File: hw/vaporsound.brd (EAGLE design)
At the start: 100 x 80 mm, 83 parts, among them P9 MA23-2, Q1 BSS138, Q2 BSS138

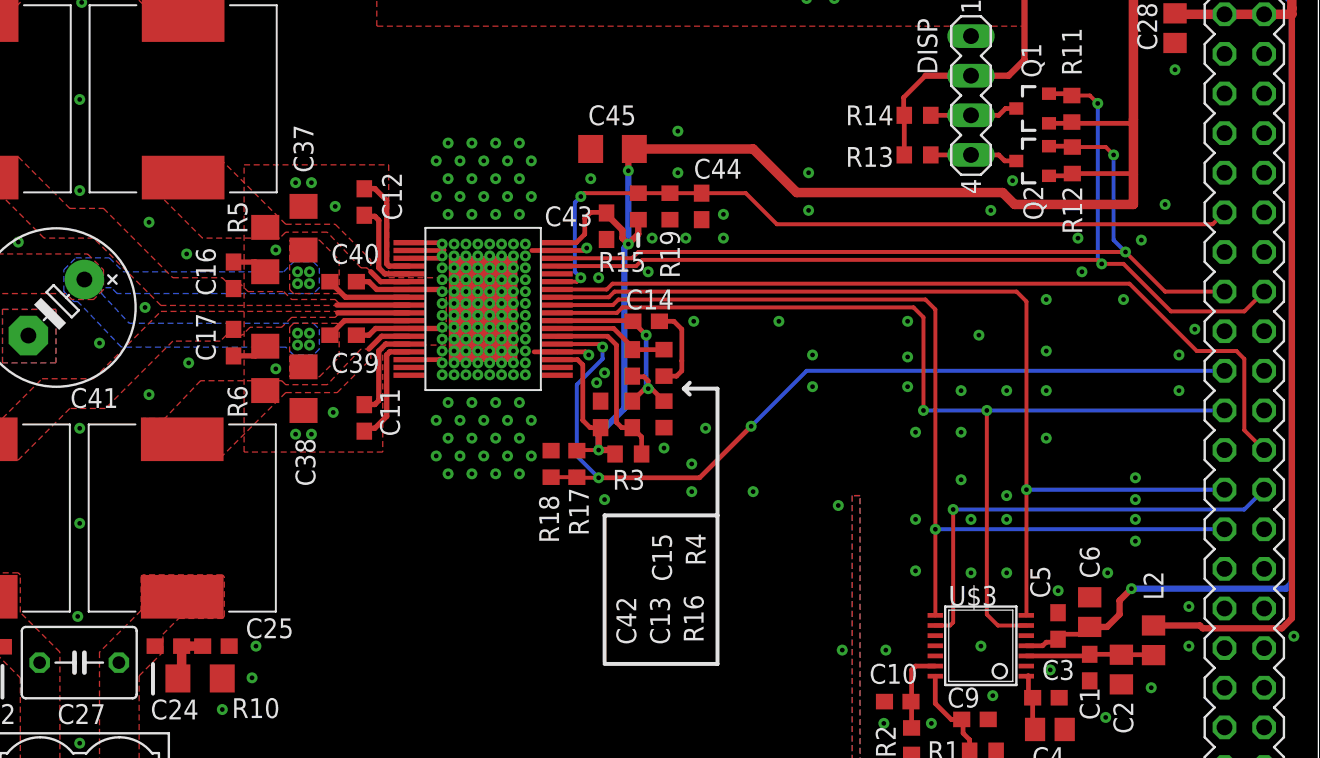
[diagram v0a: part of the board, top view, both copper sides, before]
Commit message: changes for easier manufacturability
minimum trace width 8mil
minimum clearance 7mil (8mil except the sta350bw)
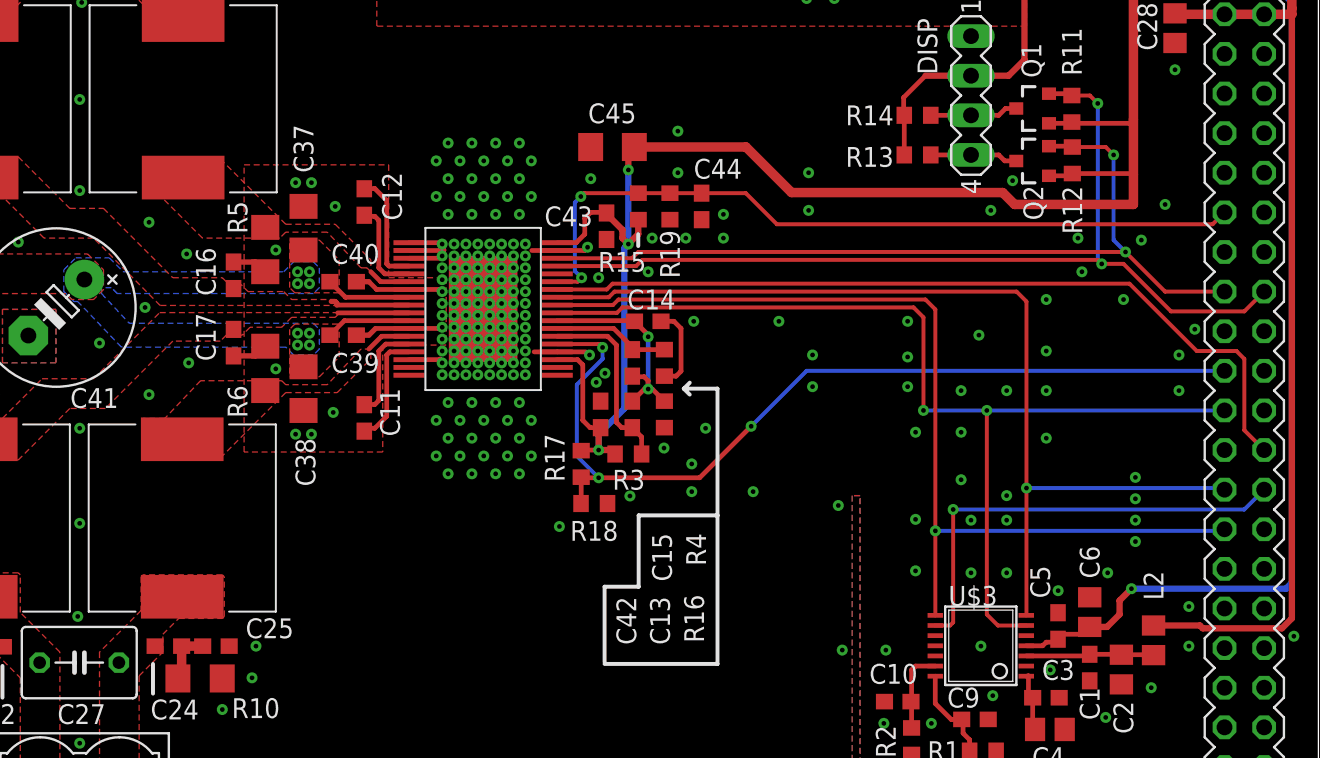
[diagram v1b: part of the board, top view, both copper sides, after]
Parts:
- moved R18 3.76 mm to (53.6, 28.3), turned to 0 degrees
- moved R17 0.28 mm to (52.7, 30.9)
- moved C45 0.13 mm to (54.7, 51.2)
- moved C14 0.10 mm to (57.0, 40.0)
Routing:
- net POWERDOWN: track 59.4 -> 58.4 mm
- net OUT2A: track 4.63 -> 5.16 mm
- net GND: track 27.0 -> 26.8 mm, vias 355 -> 356

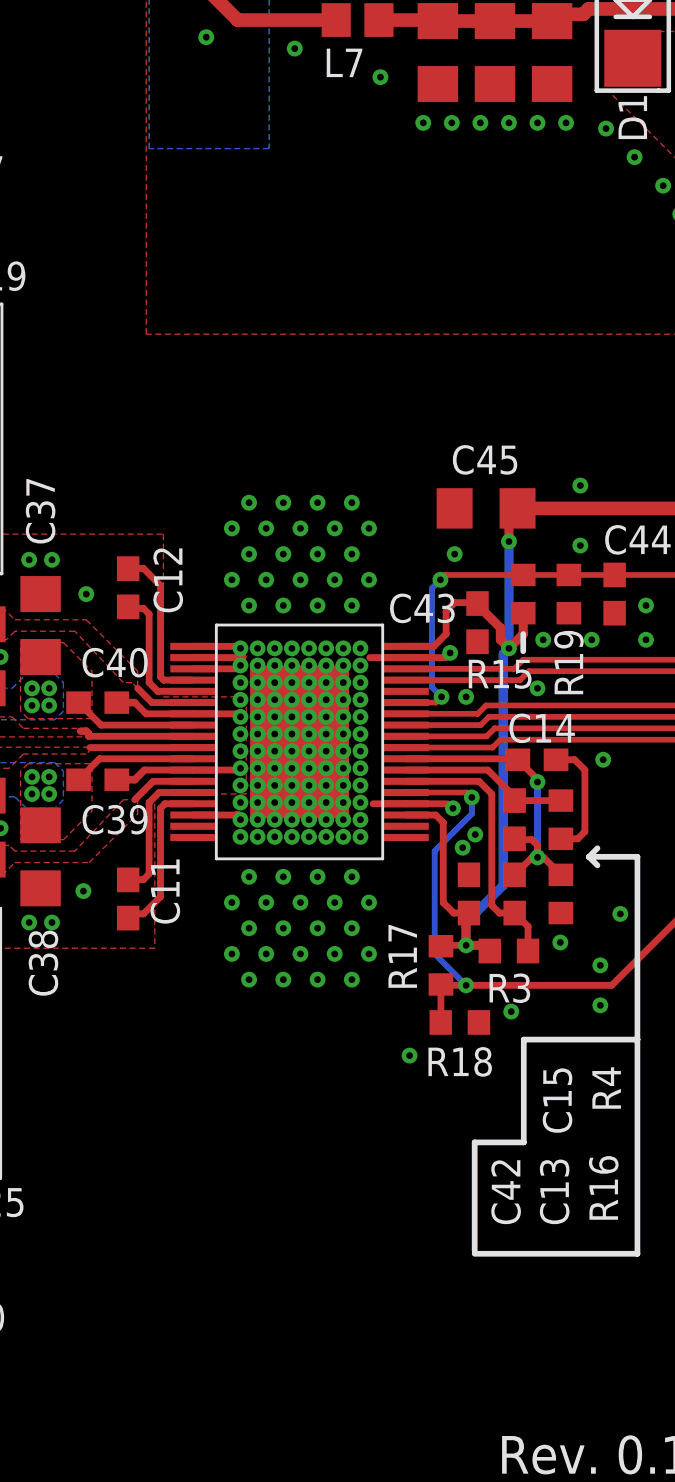
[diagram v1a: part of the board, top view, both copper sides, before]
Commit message: add more thermal vias
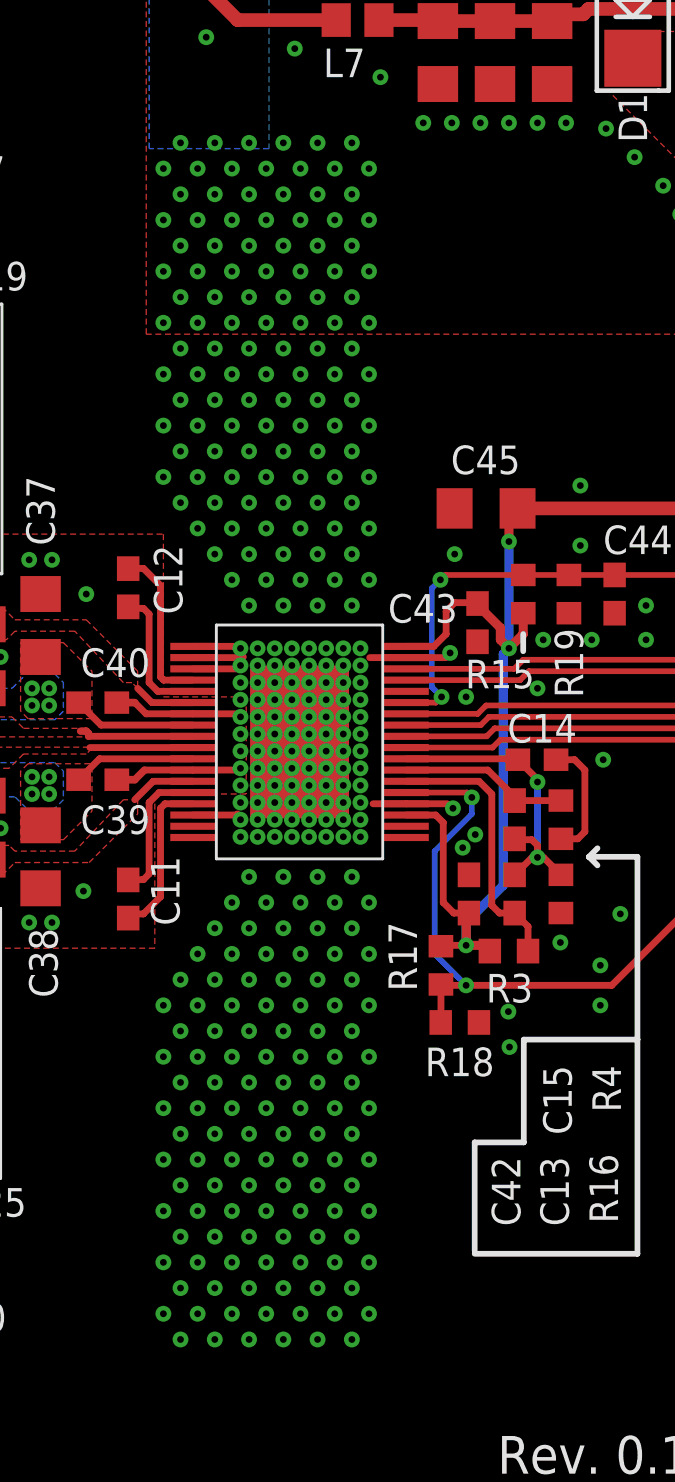
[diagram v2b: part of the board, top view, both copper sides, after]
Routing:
- net GND: vias 356 -> 546

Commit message: slightly move the sta350 to the lower end of the pcb
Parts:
- moved C12 1.02 mm to (38.8, 46.6)
- moved C14 1.02 mm to (57.0, 39.0)
- moved C41 1.02 mm to (19.1, 39.9)
- moved C44 1.02 mm to (60.5, 46.4)
- moved L4 1.02 mm to (14.0, 53.3)
- moved L5 1.02 mm to (27.2, 53.3)
- moved PWR 1.02 mm to (6.99, 39.8)
- moved R15 1.02 mm to (56.4, 46.4)
- moved R19 1.02 mm to (58.4, 46.4)
- moved R7 1.02 mm to (28.4, 63.8)
- moved R8 1.02 mm to (12.9, 63.8)
- moved SPKR2 1.02 mm to (20.6, 70.6)
- moved C27 1.02 mm to (20.5, 17.1)
- moved R17 1.02 mm to (52.7, 29.8)
- moved R18 1.02 mm to (53.6, 27.3)
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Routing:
- net SCL: track 54.9 -> 56.1 mm
- net +24V: track 99.7 -> 100.8 mm
- net MCK: track 65.1 -> 64.1 mm
- net LRCK: track 63.4 -> 62.4 mm
- net BCK: track 62.9 -> 61.8 mm
- net SDA: track 61.2 -> 62.0 mm

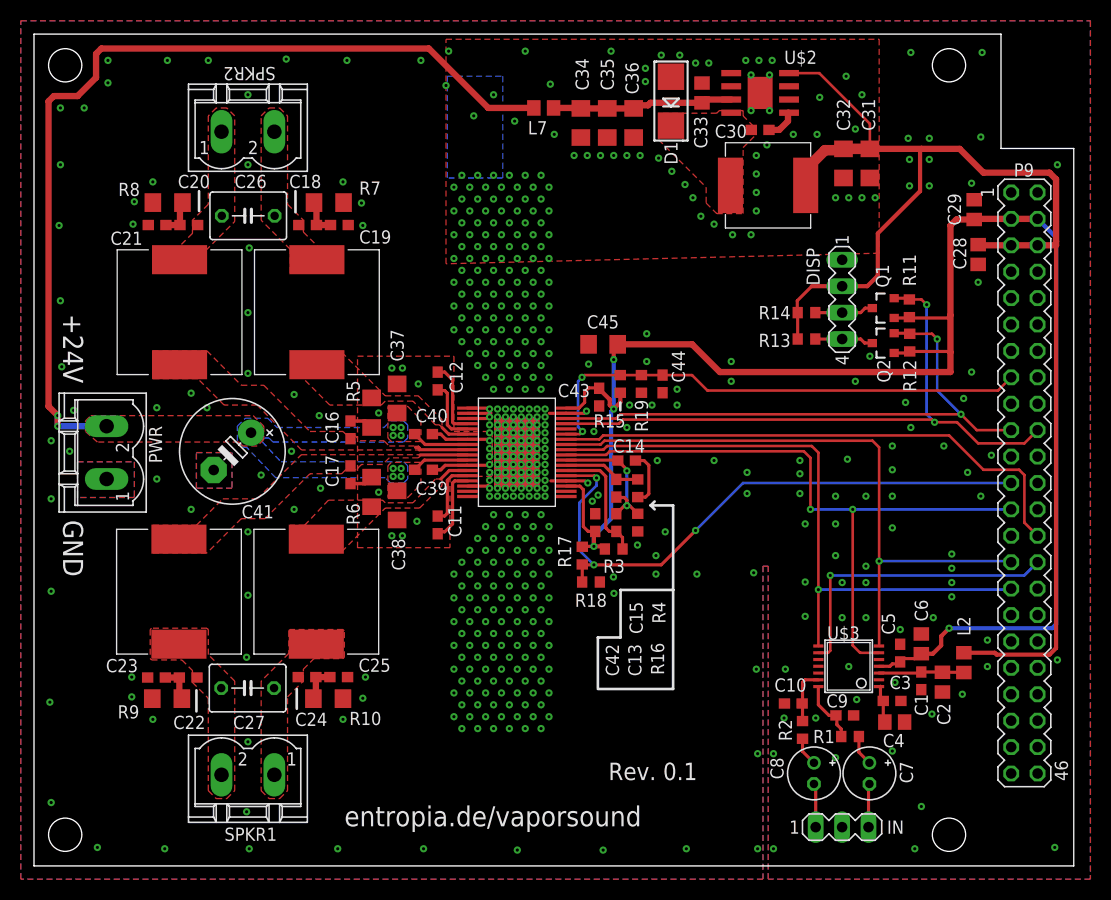
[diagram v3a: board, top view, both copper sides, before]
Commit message: add inductor name to silkscreen
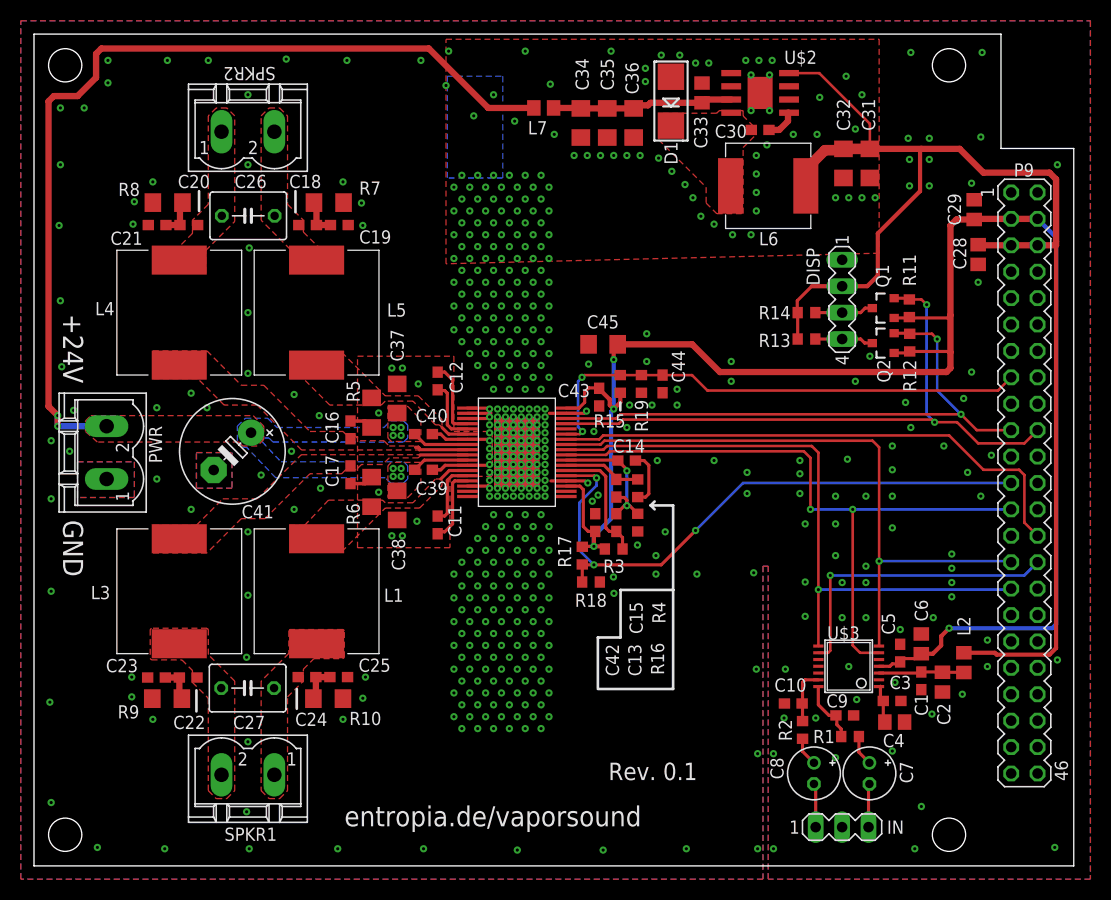
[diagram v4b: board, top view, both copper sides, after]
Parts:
- L1, L3, L4, L5: device srr1210-ind:SRR1210 -> custom-ind:SRR1210
- moved L1 0.05 mm to (27.2, 26.4)
- moved L3 0.05 mm to (14.0, 26.4)
- moved L4 0.05 mm to (14.0, 53.2)
- moved L5 0.05 mm to (27.2, 53.2)
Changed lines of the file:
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@@
 <attribute name="VALUE" x="56.1594" y="36.957" size="1.27" layer="27" rot="R270"/>
 </element>
-<element name="L1" library="srr1210-ind" package="SRR1210" value="" x="27.149" y="26.375" smashed="yes"/>
-<element name="L3" library="srr1210-ind" package="SRR1210" value="" x="13.941" y="26.375" smashed="yes"/>
-<element name="L4" library="srr1210-ind" package="SRR1210" value="" x="13.999" y="53.254" smashed="yes" rot="R180"/>
-<element name="L5" library="srr1210-ind" package="SRR1210" value="" x="27.207" y="53.254" smashed="yes" rot="R180"/>
 <element name="C16" library="rcl" package="C0603" value="330p" x="30.439" y="41.939" smashed="yes" rot="R270">
 <attribute name="NAME" x="28.026" y="43.717" size="1.27" layer="25" font="vector" ratio="14" rot="R270"/>
@@
 <attribute name="VALUE" x="70.47" y="72.691" size="1.27" layer="27" rot="R180"/>
 </element>
-<element name="L6" library="custom-ind" package="IHLP-3232DZ-11" value="" x="70.597" y="65.452" smashed="yes" rot="R90"/>
 <element name="D1" library="mircobuilder" package="SMADIODE" value="B340A-13-F" x="61.261" y="73.548" smashed="yes" rot="R90">
 <attribute name="NAME" x="61.896" y="67.452" size="1.27" layer="25" font="vector" ratio="14" rot="R90"/>
@@
 <attribute name="NAME" x="57.785" y="44.831" size="1.27" layer="25" font="vector" ratio="14" rot="R270"/>
 <attribute name="VALUE" x="60.325" y="45.72" size="1.27" layer="27" rot="R90"/>
+</element>
+<element name="L1" library="custom-ind" package="SRR1210" value="" x="27.178" y="26.416" smashed="yes">
+<attribute name="NAME" x="33.655" y="25.4" size="1.27" layer="25" font="vector" ratio="14"/>
+<attribute name="VALUE" x="22.098" y="17.526" size="1.27" layer="27"/>
+</element>
+<element name="L3" library="custom-ind" package="SRR1210" value="" x="13.97" y="26.416" smashed="yes">
+<attribute name="NAME" x="5.461" y="25.654" size="1.27" layer="25" font="vector" ratio="14"/>
+<attribute name="VALUE" x="8.89" y="17.526" size="1.27" layer="27"/>
+</element>
+<element name="L4" library="custom-ind" package="SRR1210" value="" x="13.97" y="53.213" smashed="yes" rot="R180">
+<attribute name="NAME" x="7.747" y="54.229" size="1.27" layer="25" font="vector" ratio="14" rot="R180"/>
+<attribute name="VALUE" x="19.05" y="62.103" size="1.27" layer="27" rot="R180"/>
+</element>
+<element name="L5" library="custom-ind" package="SRR1210" value="" x="27.178" y="53.213" smashed="yes" rot="R180">
+<attribute name="NAME" x="35.814" y="54.102" size="1.27" layer="25" font="vector" ratio="14" rot="R180"/>
+<attribute name="VALUE" x="32.258" y="62.103" size="1.27" layer="27" rot="R180"/>
+</element>
+<element name="L6" library="custom-ind" package="IHLP-3232DZ-11" value="" x="70.612" y="65.405" smashed="yes" rot="R90">
+<attribute name="NAME" x="69.723" y="59.69" size="1.27" layer="25" font="vector" ratio="14"/>
+<attribute name="VALUE" x="76.962" y="61.595" size="1.27" layer="27" rot="R90"/>
 </element>
 </elements>
@@
 <contactref element="C28" pad="1"/>
 <contactref element="U$2" pad="4"/>
-<contactref element="L6" pad="P$2"/>
 <contactref element="C32" pad="1"/>
 <contactref element="C31" pad="1"/>
@@
 <contactref element="R13" pad="2"/>
 <contactref element="R14" pad="2"/>
-<wire x1="74.2165" y1="65.452" x2="74.2165" y2="66.9775" width="1.016" layer="1"/>
 <wire x1="74.2165" y1="66.9775" x2="76.073" y2="68.834" width="1.016" layer="1"/>
 <wire x1="76.073" y1="68.834" x2="77.721" y2="68.834" width="1.016" layer="1"/>
@@
 <wire x1="98.298" y1="20.955" x2="98.298" y2="60.071" width="0.4064" layer="1"/>
 <wire x1="96.52" y1="59.69" x2="98.298" y2="59.69" width="0.6096" layer="1"/>
+<contactref element="L6" pad="P$2"/>
+<wire x1="74.2165" y1="66.9775" x2="74.2315" y2="66.9775" width="0.8128" layer="1"/>
+<wire x1="74.2315" y1="66.9775" x2="74.2315" y2="65.405" width="0.8128" layer="1"/>
 </signal>
 <signal name="+3V3">
@@
 <wire x1="84.222" y1="49.479" x2="88.062" y2="49.479" width="0.3048" layer="1"/>
 <wire x1="88.062" y1="49.479" x2="88.138" y2="49.403" width="0.3048" layer="1"/>
-<wire x1="65.9638" y1="47.498" x2="88.138" y2="47.498" width="0.6096" layer="1"/>
-<wire x1="88.138" y1="47.498" x2="88.138" y2="49.403" width="0.6096" layer="1"/>
+<wire x1="65.9638" y1="47.498" x2="87.757" y2="47.498" width="0.6096" layer="1"/>
+<wire x1="87.757" y1="47.498" x2="88.138" y2="47.879" width="0.6096" layer="1"/>
+<wire x1="88.138" y1="47.879" x2="88.138" y2="49.403" width="0.6096" layer="1"/>
 <wire x1="85.336" y1="20.408" x2="86.448" y2="20.408" width="0.4064" layer="1"/>
 <wire x1="86.448" y1="20.408" x2="87.249" y2="21.209" width="0.4064" layer="1"/>
@@
 <signal name="OUT2B">
 <contactref element="U$1" pad="P$6"/>
-<contactref element="L5" pad="P$1"/>
 <contactref element="R5" pad="2"/>
 <wire x1="41.691" y1="41.53" x2="39.877" y2="41.53" width="0.3048" layer="1"/>
@@
 <vertex x="24.765" y="46.99"/>
 </polygon>
+<contactref element="L5" pad="P$1"/>
 </signal>
 <signal name="OUT1A">
 <contactref element="U$1" pad="P$13"/>
-<contactref element="L1" pad="P$1"/>
 <wire x1="41.691" y1="38.03" x2="39.935" y2="38.03" width="0.3048" layer="1"/>
 <wire x1="39.935" y1="38.03" x2="39.116" y2="37.211" width="0.3048" layer="1"/>
@@
 <vertex x="24.638" y="32.766"/>
 </polygon>
+<contactref element="L1" pad="P$1"/>
 </signal>
 <signal name="SPKR2B">
 <contactref element="C18" pad="1"/>
-<contactref element="L5" pad="P$2"/>
 <contactref element="C26" pad="1"/>
 <contactref element="SPKR2" pad="2"/>
@@
 <vertex x="21.844" y="72.136"/>
 </polygon>
+<contactref element="L5" pad="P$2"/>
 </signal>
 <signal name="N$19">
@@
 </signal>
 <signal name="SPKR2A">
-<contactref element="L4" pad="P$2"/>
 <contactref element="C20" pad="1"/>
 <contactref element="C26" pad="2"/>
@@
 <vertex x="13.97" y="59.563"/>
 </polygon>
+<contactref element="L4" pad="P$2"/>
 </signal>
 <signal name="N$21">
@@
 <signal name="OUT2A">
 <contactref element="U$1" pad="P$9"/>
-<contactref element="L4" pad="P$1"/>
 <contactref element="C16" pad="2"/>
 <wire x1="41.691" y1="40.03" x2="37.059" y2="40.03" width="0.3048" layer="1"/>
@@
 <wire x1="37.059" y1="40.157" x2="36.957" y2="40.259" width="0.3302" layer="1"/>
 <wire x1="36.957" y1="40.259" x2="36.703" y2="40.259" width="0.3302" layer="1"/>
+<contactref element="L4" pad="P$1"/>
 </signal>
 <signal name="OUT1B">
 <contactref element="U$1" pad="P$10"/>
-<contactref element="L3" pad="P$1"/>
 <wire x1="41.691" y1="39.53" x2="37.117" y2="39.53" width="0.3048" layer="1"/>
 <contactref element="C17" pad="1"/>
@@
 <vertex x="21.463" y="35.306"/>
 </polygon>
+<contactref element="L3" pad="P$1"/>
 </signal>
 <signal name="SPKR1B">
-<contactref element="L3" pad="P$2"/>
 <contactref element="C22" pad="1"/>
 <contactref element="C27" pad="1"/>
@@
 <vertex x="18.542" y="6.477"/>
 </polygon>
+<contactref element="L3" pad="P$2"/>
 </signal>
 <signal name="SPKR1A">
-<contactref element="L1" pad="P$2"/>
 <contactref element="C24" pad="1"/>
 <contactref element="C27" pad="2"/>
@@
 <vertex x="21.844" y="17.78"/>
 </polygon>
+<contactref element="L1" pad="P$2"/>
 </signal>
 <signal name="N$27">
@@
 <contactref element="U$2" pad="8"/>
 <contactref element="C30" pad="2"/>
-<contactref element="L6" pad="P$1"/>
 <contactref element="D1" pad="C"/>
 <polygon width="0.2032" layer="1" thermals="no">
@@
 <vertex x="65.659" y="62.738"/>
 </polygon>
+<contactref element="L6" pad="P$1"/>
 </signal>
 <signal name="SDA5V">
